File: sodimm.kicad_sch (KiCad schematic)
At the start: 11 parts, among them J1 PCB-Edge_SODIMM_144_SDR

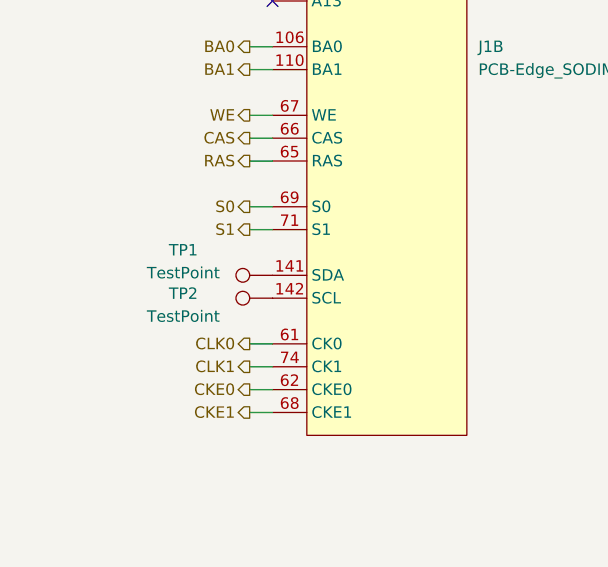
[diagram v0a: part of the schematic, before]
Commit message: [#100650] Add EEPROM memory IC for Serial Presence Detection
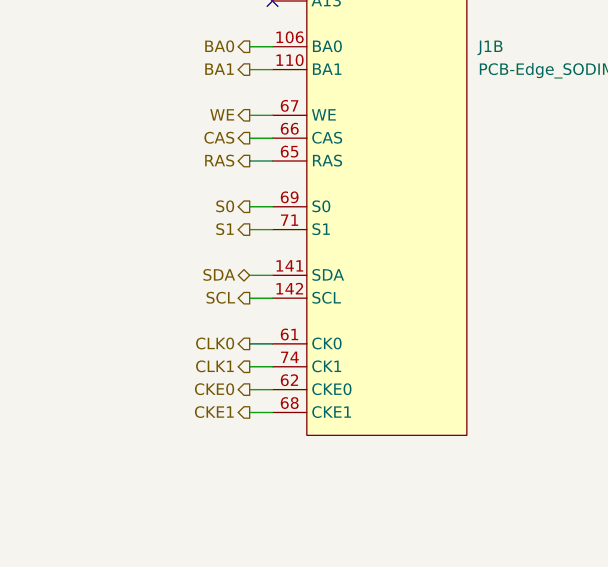
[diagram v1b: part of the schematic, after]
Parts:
- removed TP1, TP2: TestPoint, symbol Connector:TestPoint
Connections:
- net SDA: now reaches J1.141 (SDA)
- net SCL: now reaches J1.142 (SCL)

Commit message: [#100650] Update schematic labels, add bulk cap
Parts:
- added C66: C_10u_0402, antmicro-footprints:C_0402_1005Metric, symbol antmicroCapacitors0402:C_10u_0402
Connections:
- net +3.3V: now also C66.1
- net GND: now also C66.2

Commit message: [#100650] Update PCB layout
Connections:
- net D0: now also R1.5 (R4.2); no longer R1.1 (R1.1)
- net D1: now also R1.6 (R3.2); no longer R1.2 (R2.1)
- net D10: now also R3.7 (R2.2); no longer R3.3 (R3.1)
- net D11: now also R3.8 (R1.2); no longer R3.4 (R4.1)
- net D12: now also R4.5 (R4.2); no longer R4.1 (R1.1)
- net D13: now also R4.6 (R3.2); no longer R4.2 (R2.1)
- net D14: now also R4.7 (R2.2); no longer R4.3 (R3.1)
- net D15: now also R4.8 (R1.2); no longer R4.4 (R4.1)
- net D16: now also R5.5 (R4.2); no longer R5.1 (R1.1)
- net D17: now also R5.6 (R3.2); no longer R5.2 (R2.1)
- net D18: now also R5.7 (R2.2); no longer R5.3 (R3.1)
- net D19: now also R5.8 (R1.2); no longer R5.4 (R4.1)
- net D2: now also R1.7 (R2.2); no longer R1.3 (R3.1)
- net D20: now also R6.5 (R4.2); no longer R6.1 (R1.1)
- net D21: now also R6.6 (R3.2); no longer R6.2 (R2.1)
- net D22: now also R6.7 (R2.2); no longer R6.3 (R3.1)
- net D23: now also R6.8 (R1.2); no longer R6.4 (R4.1)
- net D24: now also R7.5 (R4.2); no longer R7.1 (R1.1)
- net D25: now also R7.6 (R3.2); no longer R7.2 (R2.1)
- net D26: now also R7.7 (R2.2); no longer R7.3 (R3.1)
- net D27: now also R7.8 (R1.2); no longer R7.4 (R4.1)
- net D28: now also R8.5 (R4.2); no longer R8.1 (R1.1)
- net D29: now also R8.6 (R3.2); no longer R8.2 (R2.1)
- net D3: now also R1.8 (R1.2); no longer R1.4 (R4.1)
- net D30: now also R8.7 (R2.2); no longer R8.3 (R3.1)
- net D31: now also R8.8 (R1.2); no longer R8.4 (R4.1)
- net D4: now also R2.5 (R4.2); no longer R2.1 (R1.1)
- net D5: now also R2.6 (R3.2); no longer R2.2 (R2.1)
- net D6: now also R2.7 (R2.2); no longer R2.3 (R3.1)
- net D7: now also R2.8 (R1.2); no longer R2.4 (R4.1)
- net D8: now also R3.5 (R4.2); no longer R3.1 (R1.1)
- net D9: now also R3.6 (R3.2); no longer R3.2 (R2.1)
- net at J1.99 (DQ23): now also R6.4 (R4.1); no longer R6.5 (R4.2)
- net at J1.97 (DQ22): now also R6.3 (R3.1); no longer R6.6 (R3.2)
- net at J1.95 (DQ21): now also R6.2 (R2.1); no longer R6.7 (R2.2)
- net at J1.93 (DQ20): now also R6.1 (R1.1); no longer R6.8 (R1.2)
- net at J1.19 (DQ7): now also R2.4 (R4.1); no longer R2.5 (R4.2)
- net at J1.17 (DQ6): now also R2.3 (R3.1); no longer R2.6 (R3.2)
- net at J1.15 (DQ5): now also R2.2 (R2.1); no longer R2.7 (R2.2)
- net at J1.13 (DQ4): now also R2.1 (R1.1); no longer R2.8 (R1.2)
- net at J1.127 (DQ27): now also R7.4 (R4.1); no longer R7.5 (R4.2)
- net at J1.125 (DQ26): now also R7.3 (R3.1); no longer R7.6 (R3.2)
- net at J1.123 (DQ25): now also R7.2 (R2.1); no longer R7.7 (R2.2)
- net at J1.121 (DQ24): now also R7.1 (R1.1); no longer R7.8 (R1.2)
- net at J1.131 (DQ28): now also R8.1 (R1.1); no longer R8.8 (R1.2)
- net at J1.133 (DQ29): now also R8.2 (R2.1); no longer R8.7 (R2.2)
- net at J1.135 (DQ30): now also R8.3 (R3.1); no longer R8.6 (R3.2)
- net at J1.137 (DQ31): now also R8.4 (R4.1); no longer R8.5 (R4.2)
- net at J1.3 (DQ0): now also R1.1 (R1.1); no longer R1.8 (R1.2)
- net at J1.37 (DQ8): now also R3.1 (R1.1); no longer R3.8 (R1.2)
- net at J1.39 (DQ9): now also R3.2 (R2.1); no longer R3.7 (R2.2)
- net at J1.41 (DQ10): now also R3.3 (R3.1); no longer R3.6 (R3.2)
- net at J1.43 (DQ11): now also R3.4 (R4.1); no longer R3.5 (R4.2)
- net at J1.47 (DQ12): now also R4.1 (R1.1); no longer R4.8 (R1.2)
- net at J1.49 (DQ13): now also R4.2 (R2.1); no longer R4.7 (R2.2)
- net at J1.5 (DQ1): now also R1.2 (R2.1); no longer R1.7 (R2.2)
- net at J1.51 (DQ14): now also R4.3 (R3.1); no longer R4.6 (R3.2)
- net at J1.53 (DQ15): now also R4.4 (R4.1); no longer R4.5 (R4.2)
- net at J1.7 (DQ2): now also R1.3 (R3.1); no longer R1.6 (R3.2)
- net at J1.83 (DQ16): now also R5.1 (R1.1); no longer R5.8 (R1.2)
- net at J1.85 (DQ17): now also R5.2 (R2.1); no longer R5.7 (R2.2)
- net at J1.87 (DQ18): now also R5.3 (R3.1); no longer R5.6 (R3.2)
- net at J1.89 (DQ19): now also R5.4 (R4.1); no longer R5.5 (R4.2)
- net at J1.9 (DQ3): now also R1.4 (R4.1); no longer R1.5 (R4.2)

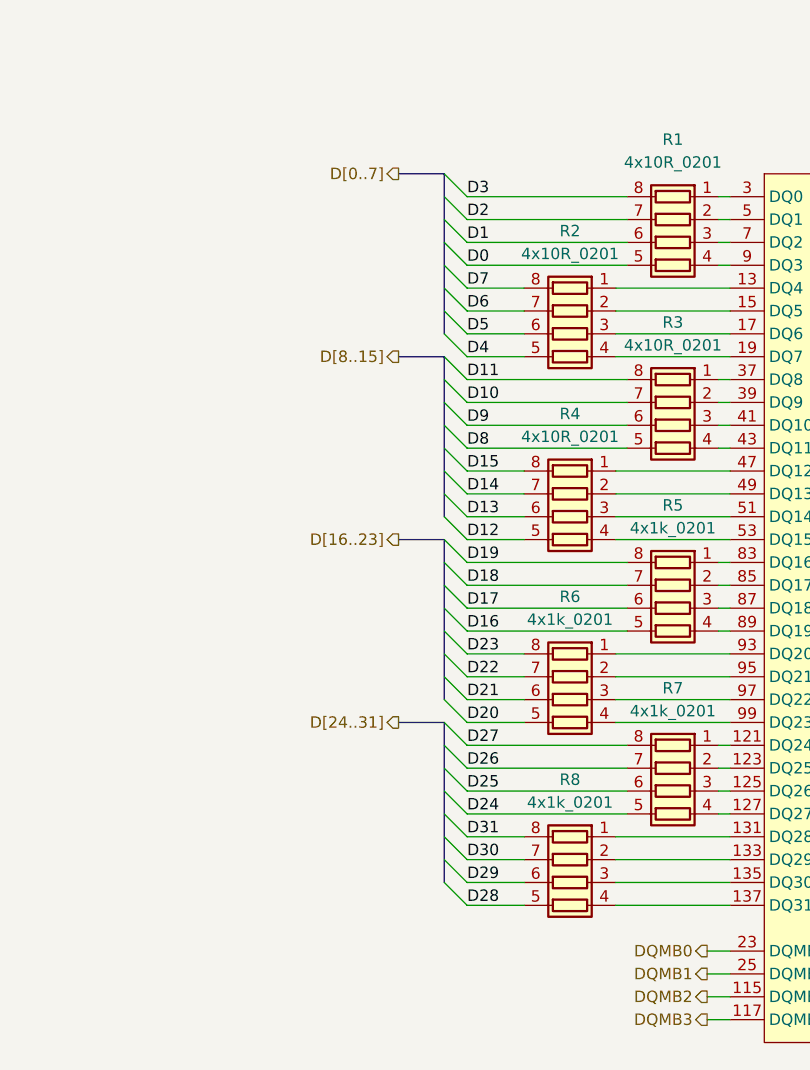
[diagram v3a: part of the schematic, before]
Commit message: [#100919] Route data bus
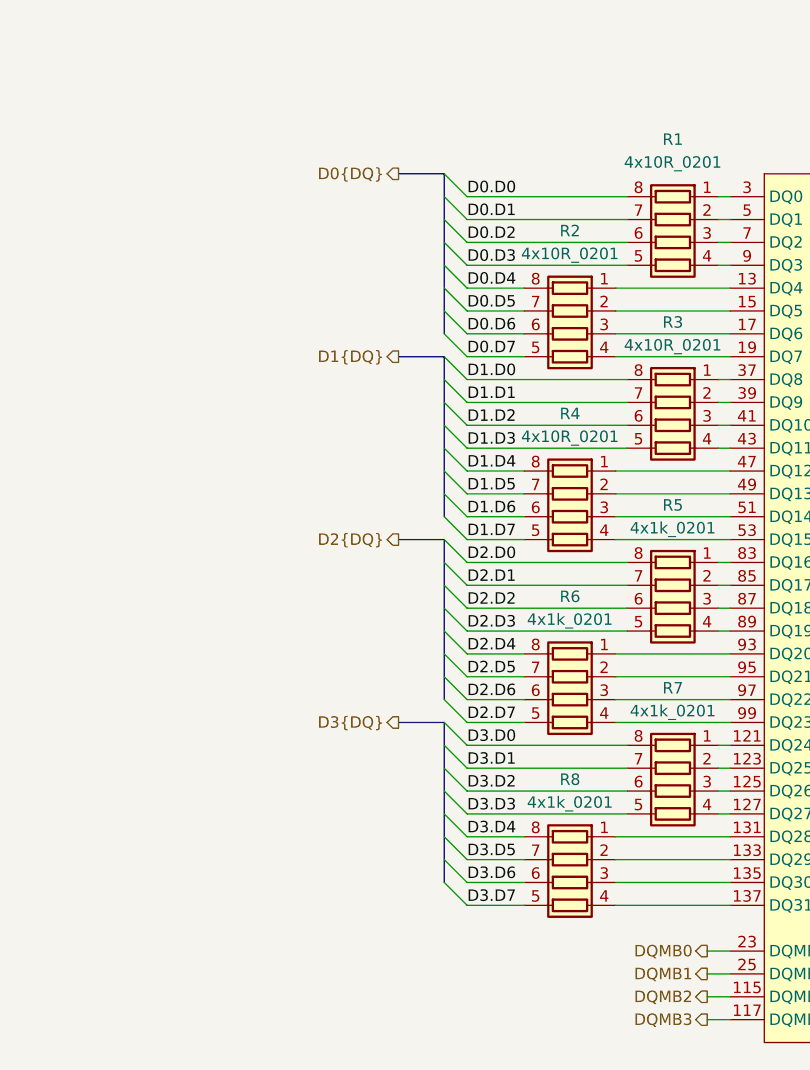
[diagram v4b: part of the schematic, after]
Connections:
- net D0 renamed D0.D3
- net D1 renamed D0.D2
- net D10 renamed D1.D1
- net D11 renamed D1.D0
- net D12 renamed D1.D7
- net D13 renamed D1.D6
- net D14 renamed D1.D5
- net D15 renamed D1.D4
- net D16 renamed D2.D3
- net D17 renamed D2.D2
- net D18 renamed D2.D1
- net D19 renamed D2.D0
- net D2 renamed D0.D1
- net D20 renamed D2.D7
- net D21 renamed D2.D6
- net D22 renamed D2.D5
- net D23 renamed D2.D4
- net D24 renamed D3.D3
- net D25 renamed D3.D2
- net D26 renamed D3.D1
- net D27 renamed D3.D0
- net D28 renamed D3.D7
- net D29 renamed D3.D6
- net D3 renamed D0.D0
- net D30 renamed D3.D5
- net D31 renamed D3.D4
- net D4 renamed D0.D7
- net D5 renamed D0.D6
- net D6 renamed D0.D5
- net D7 renamed D0.D4
- net D8 renamed D1.D3
- net D9 renamed D1.D2

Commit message: [#100919] Add test points
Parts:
- added TP2, TP3: TP_1mm_SMD, antmicro-footprints:TP_SMD_1mm, symbol antmicroTestPoints:TP_1mm_SMD
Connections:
- net +3.3V: now also TP2.1
- net GND: now also TP3.1
